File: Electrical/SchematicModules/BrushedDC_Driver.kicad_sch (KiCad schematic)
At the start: 7 parts, among them U4 MAX22201

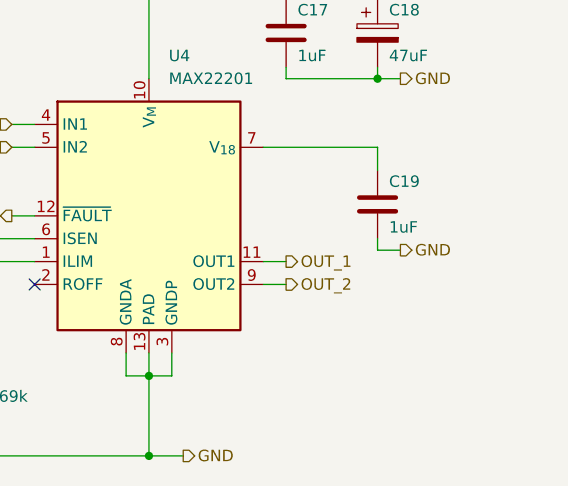
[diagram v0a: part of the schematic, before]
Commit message: Added layout for prototype 1
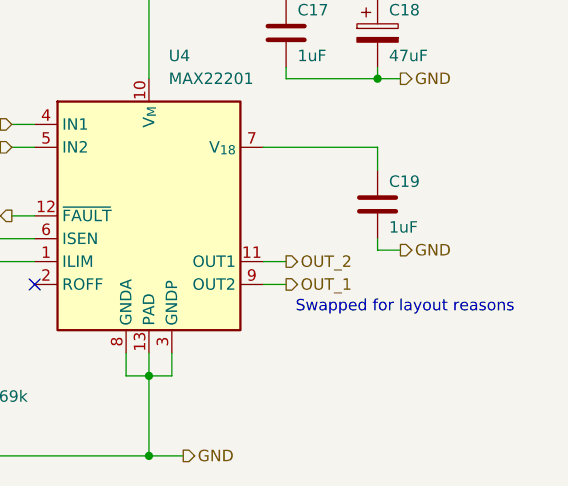
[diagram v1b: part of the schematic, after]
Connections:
- net OUT_1: now also U4.9 (OUT2); no longer U4.11 (OUT1)
- net OUT_2: now also U4.11 (OUT1); no longer U4.9 (OUT2)
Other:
- note added: "Swapped for layout reasons"
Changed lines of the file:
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@@
+		)
+	)
+	(text "Swapped for layout reasons"
+		(exclude_from_sim no)
+		(at 174.498 111.76 0)
+		(effects
+			(font
+				(size 1.27 1.27)
+			)
 		)
 	)
@@
 	(hierarchical_label "OUT_2"
 		(shape output)
-		(at 161.29 109.22 0)
+		(at 161.29 106.68 0)
 		(fields_autoplaced yes)
 		(effects
@@
 	(hierarchical_label "OUT_1"
 		(shape output)
-		(at 161.29 106.68 0)
+		(at 161.29 109.22 0)
 		(fields_autoplaced yes)
 		(effects

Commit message: Finalizing the layout
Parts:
- C18: now not fitted
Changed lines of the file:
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@@
 		(exclude_from_sim no)
 		(in_bom yes)
-		(on_board yes)
-		(dnp no)
+		(on_board no)
+		(dnp yes)
 		(property "Reference" "C18"
 			(at 172.72 78.74 0)
